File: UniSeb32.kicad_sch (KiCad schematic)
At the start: 55 parts, among them J1 IO, J101 Micro_SD_Card_Det, J2 ARJM11C7-114-BA-EW2, J3 Conn_02x05_Odd_Even, J6 SDS011, J7 Conn_01x02_Female, J8 Conn_01x02_Female, U1 mini_esp32, U101 RTL8201F-VB-CG, U3 AMS1117-3.3, U4 AMS5915, U5 module_bme280, U6 RT9400, U7 MCP23008-xSS, U8 HLK-PM01, X1 233-508, X2 233-503, X3 233-504

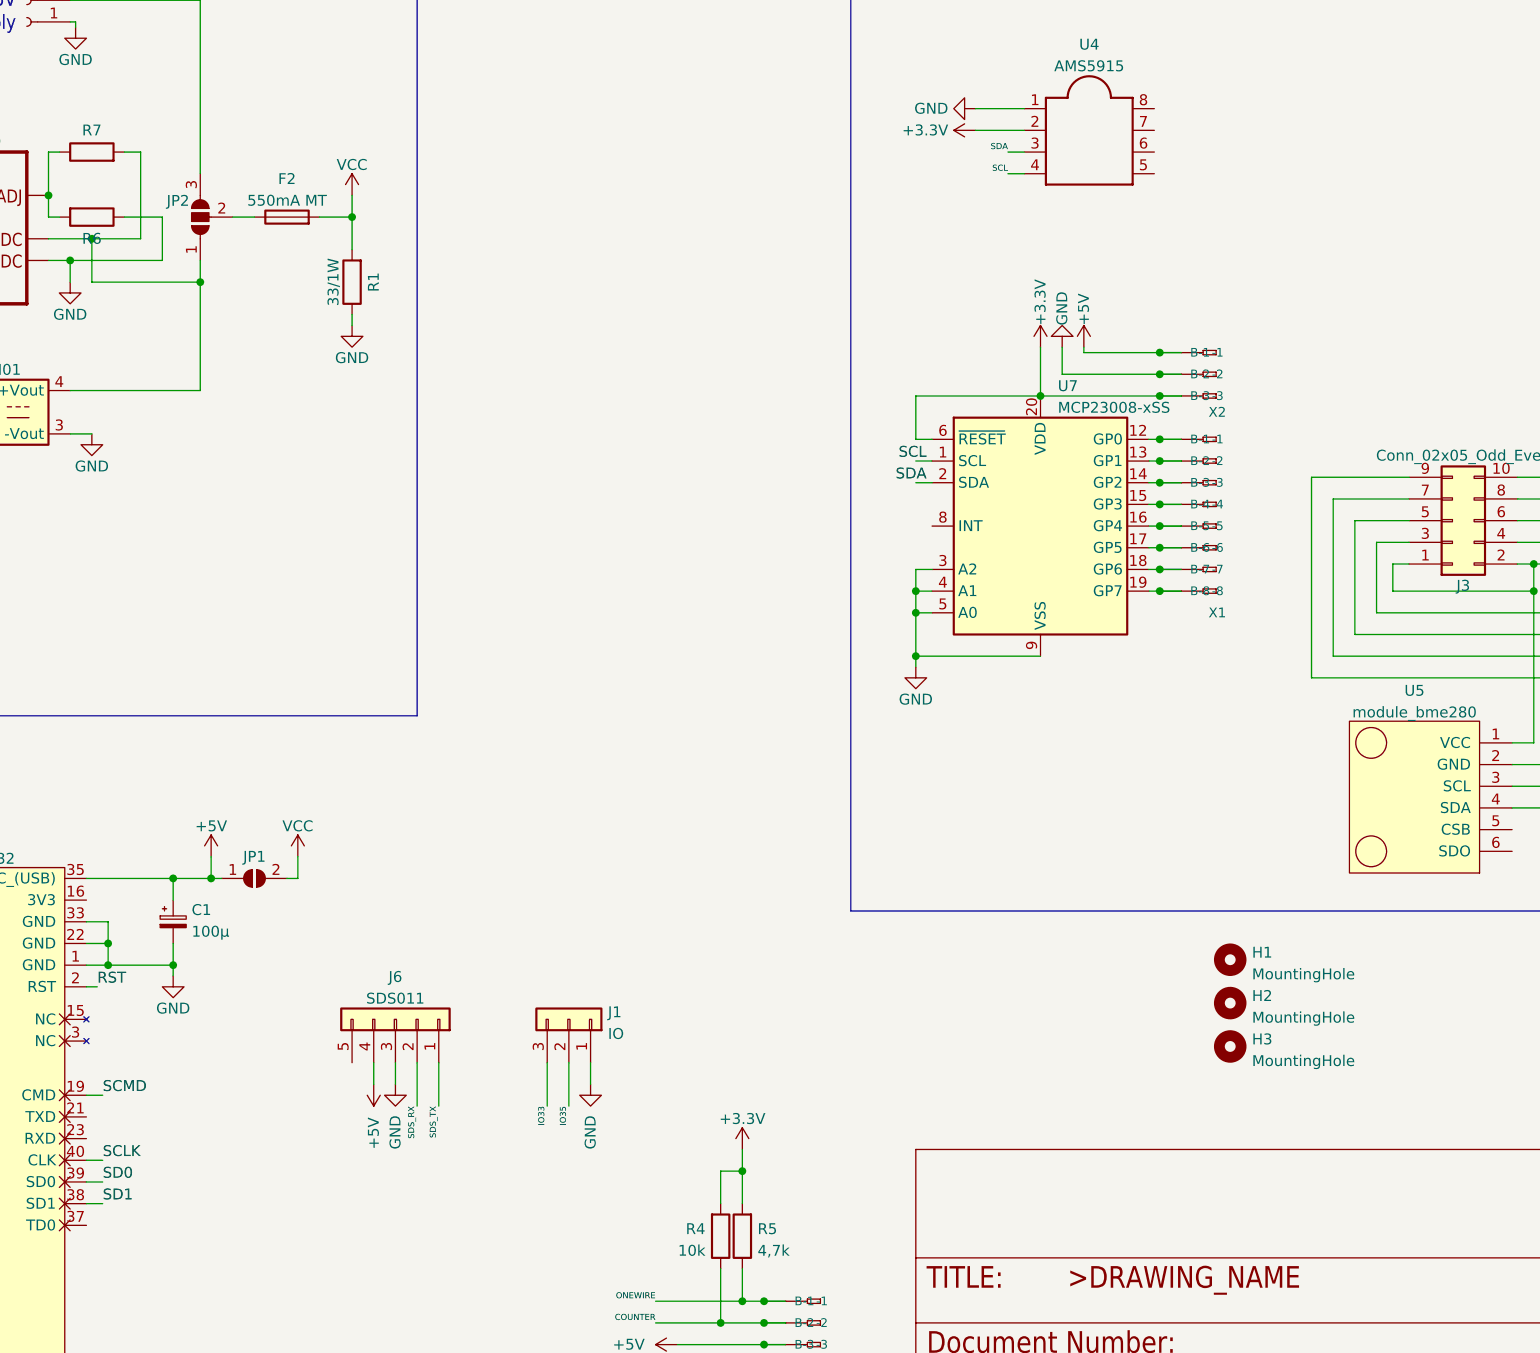
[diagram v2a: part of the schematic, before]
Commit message: removed SJ1, rename SJ2 -> SJ1, added SJ2 to change pin2 usage of J1
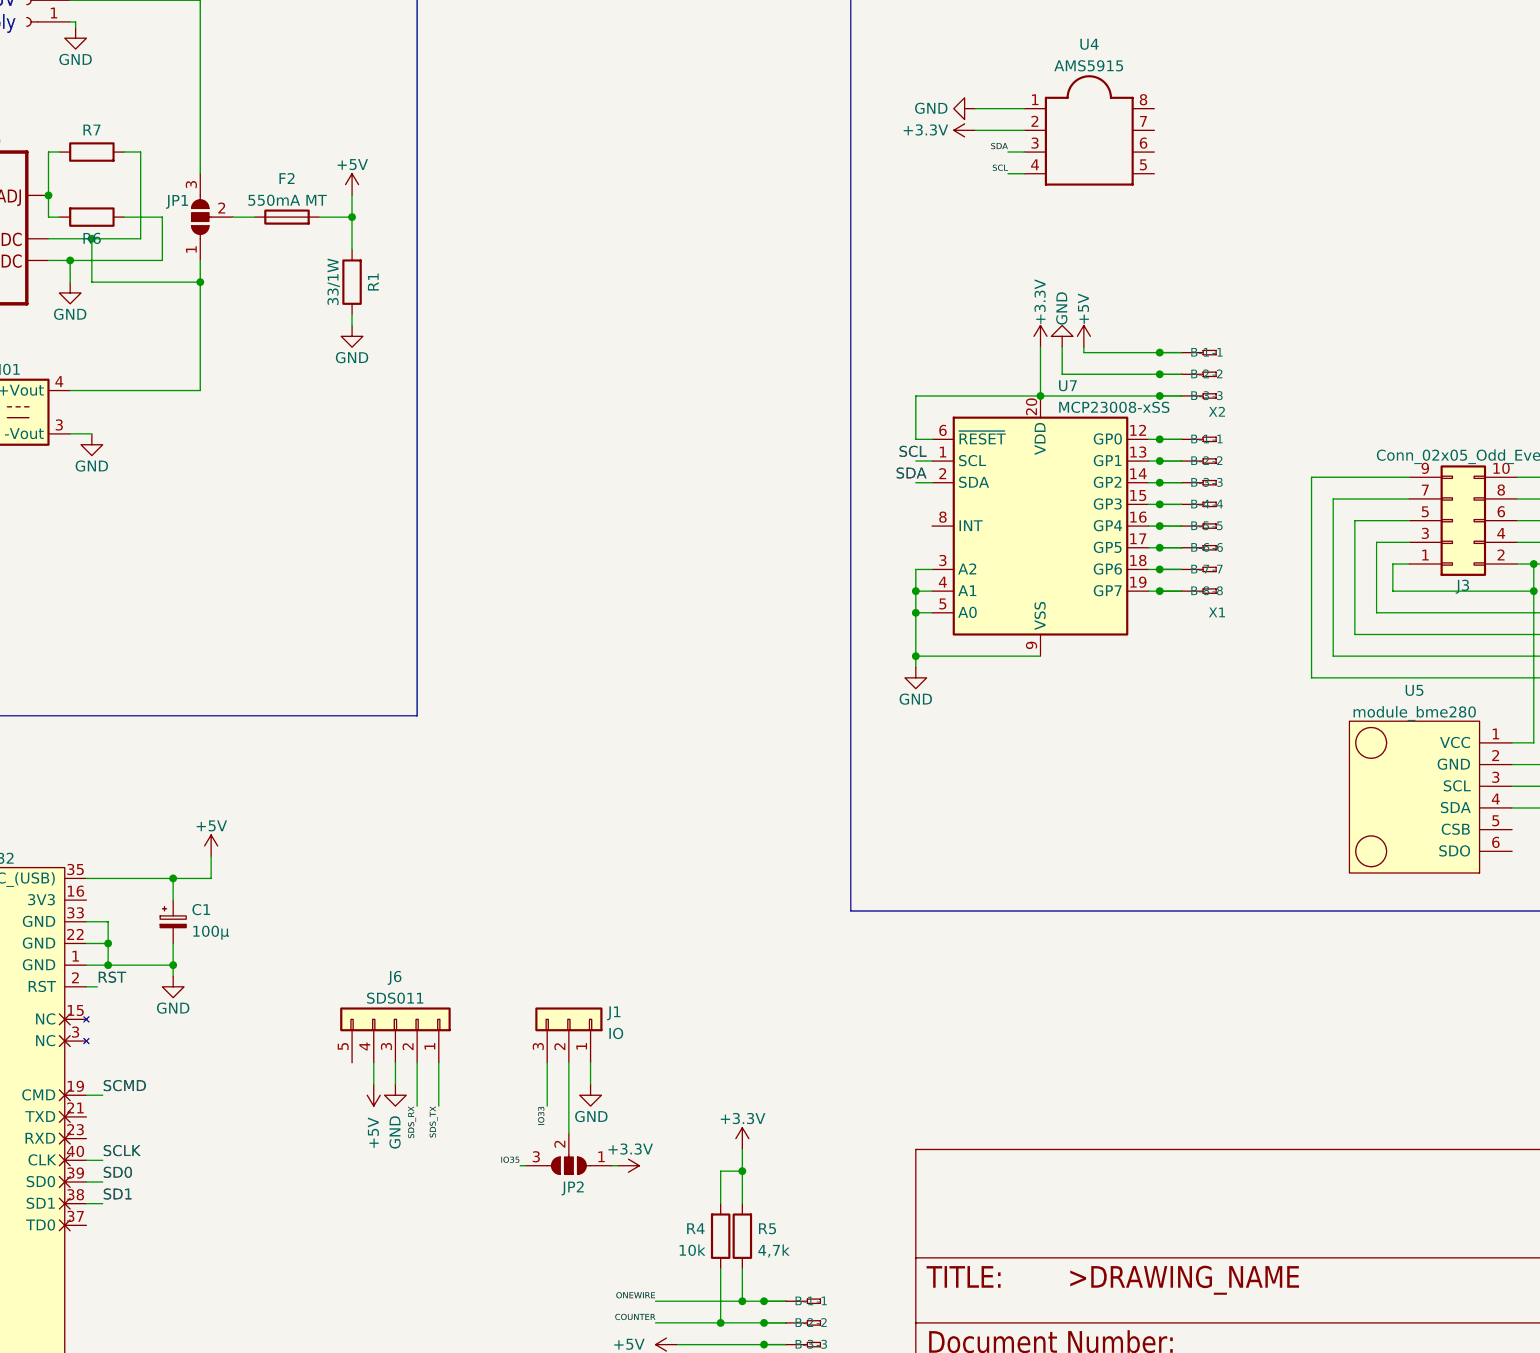
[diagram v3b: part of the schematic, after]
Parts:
- removed H1, H2, H3: MountingHole, MountingHole:MountingHole_3.2mm_M3, symbol Mechanical:MountingHole
- removed JP1: SolderJumper_2_Open, Jumper:SolderJumper-2_P1.3mm_Open_Pad1.0x1.5mm, symbol Jumper:SolderJumper_2_Open
- added JP2: SolderJumper_3_Open, Jumper:SolderJumper-3_P1.3mm_Open_Pad1.0x1.5mm_NumberLabels, symbol Jumper:SolderJumper_3_Open
- renumbered JP2 to JP1
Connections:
- net VCC is gone; now on net +5V: F2.2, R1.2
- net +3.3V: now also JP2.1 (A)
- net IO35: now also JP2.3 (B); no longer J1.2 (Pin_2)
- new net: J1.2 (Pin_2), JP2.2 (C)

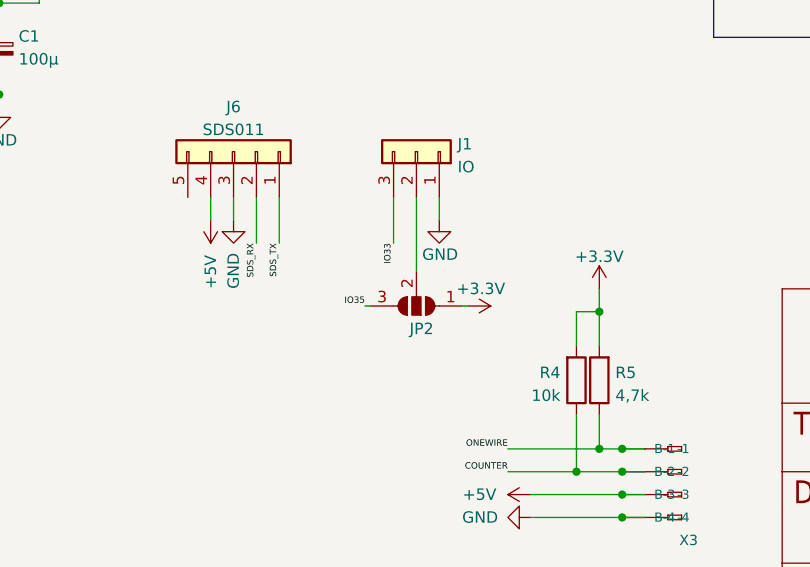
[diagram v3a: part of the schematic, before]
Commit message: added pullup for pin3 of J1
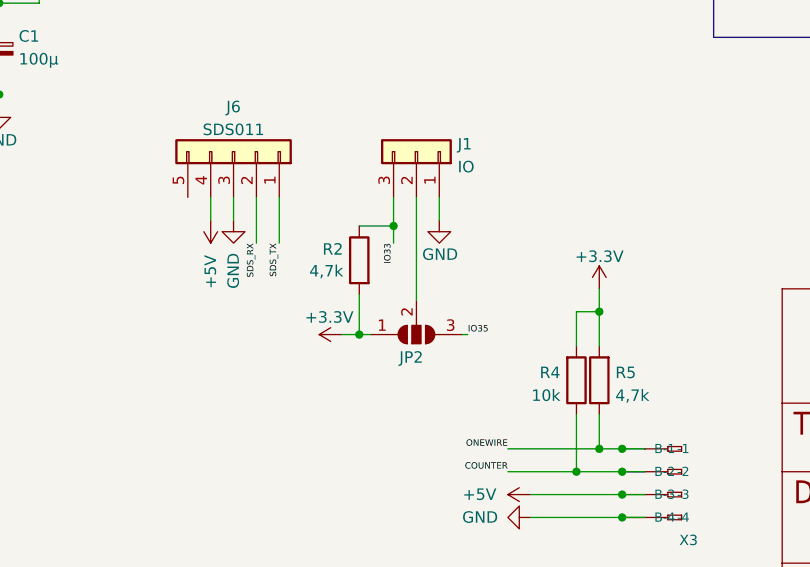
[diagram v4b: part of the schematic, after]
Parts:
- added R2: 4,7k, Resistor_SMD:R_0603_1608Metric, symbol Device:R
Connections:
- net +3.3V: now also R2.2
- net IO33: now also R2.1
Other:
- moved on the sheet: JP2
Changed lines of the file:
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@@
   (junction (at 124.46 259.08) (diameter 0) (color 0 0 0 0)
   )
+  (junction (at 133.35 167.64) (diameter 0) (color 0 0 0 0)
+  )
   (junction (at 260.35 86.36) (diameter 0) (color 0 0 0 0)
   )
@@
   (junction (at 78.74 50.8) (diameter 0) (color 0 0 0 0)
   )
+  (junction (at 137.16 155.575) (diameter 0) (color 0 0 0 0)
+  )
   (junction (at 208.915 97.155) (diameter 0) (color 0 0 0 0)
   )
@@
     (stroke (width 0) (type default))
   )
-  (wire (pts (xy 145.415 164.465) (xy 144.78 164.465))
+  (wire (pts (xy 131.445 167.64) (xy 133.35 167.64))
     (stroke (width 0) (type default))
   )
@@
     (stroke (width 0) (type default))
   )
+  (wire (pts (xy 133.35 155.575) (xy 137.16 155.575))
+    (stroke (width 0) (type default))
+  )
   (wire (pts (xy 173.355 269.24) (xy 173.355 273.685))
     (stroke (width 0) (type default))
   )
+  (wire (pts (xy 133.35 167.64) (xy 134.62 167.64))
+    (stroke (width 0) (type default))
+  )
   (wire (pts (xy 145.415 280.67) (xy 152.4 280.67))
     (stroke (width 0) (type default))
@@
     (stroke (width 0) (type default))
   )
-  (wire (pts (xy 139.7 152.4) (xy 139.7 160.655))
+  (wire (pts (xy 139.7 152.4) (xy 139.7 163.83))
     (stroke (width 0) (type default))
   )
@@
     (stroke (width 0) (type default))
   )
-  (wire (pts (xy 133.985 164.465) (xy 134.62 164.465))
+  (wire (pts (xy 145.415 167.64) (xy 144.78 167.64))
     (stroke (width 0) (type default))
   )
@@
     (stroke (width 0) (type default))
   )
-  (wire (pts (xy 137.16 152.4) (xy 137.16 157.48))
+  (wire (pts (xy 137.16 152.4) (xy 137.16 155.575))
     (stroke (width 0) (type default))
   )
@@
     (stroke (width 0) (type default))
   )
+  (wire (pts (xy 133.35 163.195) (xy 133.35 167.64))
+    (stroke (width 0) (type default))
+  )
   (wire (pts (xy 53.975 179.07) (xy 56.515 179.07))
     (stroke (width 0) (type default))
@@
     (stroke (width 0) (type default))
   )
+  (wire (pts (xy 137.16 155.575) (xy 137.16 157.48))
+    (stroke (width 0) (type default))
+  )
   (wire (pts (xy 137.16 335.915) (xy 137.16 337.185))
     (stroke (width 0) (type default))
@@
     (effects (font (size 1.27 1.27)) (justify left bottom))
   )
-  (label "IO35" (at 133.985 164.465 180) (fields_autoplaced)
-    (effects (font (size 0.7112 0.7112)) (justify right bottom))
+  (label "IO35" (at 145.415 167.64 0) (fields_autoplaced)
+    (effects (font (size 0.7112 0.7112)) (justify left bottom))
   )
   (label "IO0" (at 55.245 130.81 180) (fields_autoplaced)
@@
     )
   )
-  (symbol (lib_id "Jumper:SolderJumper_3_Open") (at 139.7 164.465 180) (unit 1)
+  (symbol (lib_id "Jumper:SolderJumper_3_Open") (at 139.7 167.64 0) (mirror x) (unit 1)
     (in_bom yes) (on_board yes) (dnp no)
-    (property "Reference" "JP2" (at 141.605 167.005 0)
+    (property "Reference" "JP2" (at 137.795 170.18 0)
       (effects (font (size 1.27 1.27)) (justify left))
     )
-    (property "Value" "SolderJumper_3_Open" (at 141.4022 166.1159 90)
+    (property "Value" "SolderJumper_3_Open" (at 137.9978 169.2909 90)
       (effects (font (size 1.27 1.27)) (justify left) hide)
     )
-    (property "Footprint" "Jumper:SolderJumper-3_P1.3mm_Open_Pad1.0x1.5mm_NumberLabels" (at 139.7 164.465 0)
+    (property "Footprint" "Jumper:SolderJumper-3_P1.3mm_Open_Pad1.0x1.5mm_NumberLabels" (at 139.7 167.64 0)
       (effects (font (size 1.27 1.27)) hide)
     )
-    (property "Datasheet" "~" (at 139.7 164.465 0)
+    (property "Datasheet" "~" (at 139.7 167.64 0)
       (effects (font (size 1.27 1.27)) hide)
     )
@@
     )
   )
-  (symbol (lib_id "power:+3.3V") (at 145.415 164.465 270) (unit 1)
+  (symbol (lib_id "power:+3.3V") (at 131.445 167.64 90) (mirror x) (unit 1)
     (in_bom yes) (on_board yes) (dnp no)
-    (property "Reference" "#PWR03" (at 141.605 164.465 0)
+    (property "Reference" "#PWR03" (at 135.255 167.64 0)
       (effects (font (size 1.27 1.27)) hide)
     )
-    (property "Value" "+3.3V" (at 144.145 162.56 90)
+    (property "Value" "+3.3V" (at 132.715 165.735 90)
       (effects (font (size 1.27 1.27)) (justify left))
     )
-    (property "Footprint" "" (at 145.415 164.465 0)
+    (property "Footprint" "" (at 131.445 167.64 0)
       (effects (font (size 1.27 1.27)) hide)
     )
-    (property "Datasheet" "" (at 145.415 164.465 0)
+    (property "Datasheet" "" (at 131.445 167.64 0)
       (effects (font (size 1.27 1.27)) hide)
     )
@@
         )
       )
+    )
+  )
+  (symbol (lib_id "Device:R") (at 133.35 159.385 0) (mirror y) (unit 1)
+    (in_bom yes) (on_board yes) (dnp no)
+    (property "Reference" "R2" (at 131.572 158.1729 0)
+      (effects (font (size 1.27 1.27)) (justify left))
+    )
+    (property "Value" "4,7k" (at 131.572 160.5971 0)
+      (effects (font (size 1.27 1.27)) (justify left))
+    )
+    (property "Footprint" "Resistor_SMD:R_0603_1608Metric" (at 135.128 159.385 90)
+      (effects (font (size 1.27 1.27)) hide)
+    )
+    (property "Datasheet" "~" (at 133.35 159.385 0)
+      (effects (font (size 1.27 1.27)) hide)
+    )
+    (property "LCSC" "C23162" (at 133.35 159.385 90)
+      (effects (font (size 1.27 1.27)) hide)
+    )
+    (property "JLC" "0603" (at 133.35 159.385 0)
+      (effects (font (size 1.27 1.27)) hide)
+    )
+    (pin "1")
+    (pin "2")
+    (instances
+      (project "UniSeb32"
+        (path "/94c30dae-83f2-410e-815e-9e5d06243376"
+          (reference "R2") (unit 1)
+        )
+      )

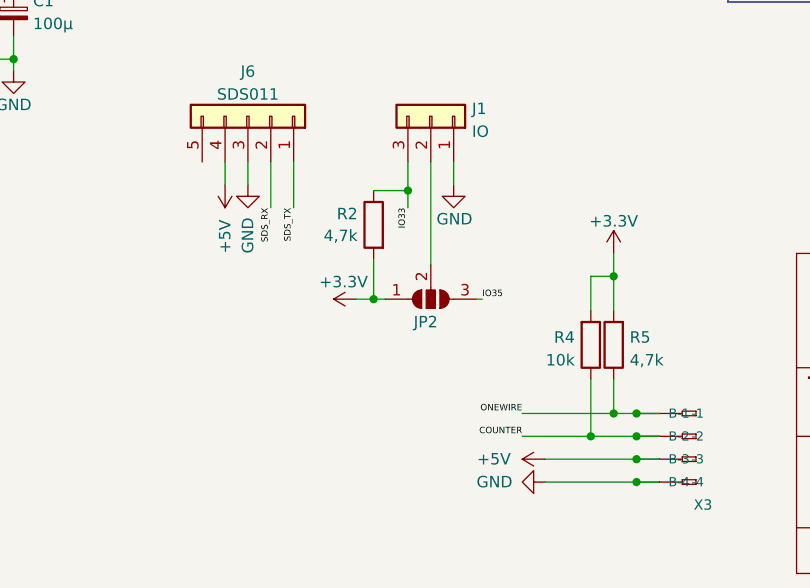
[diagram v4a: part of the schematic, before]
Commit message: Changed JP2-fixed voltage option (3.3V) to flexible voltage (3.3V/5V) with JP3
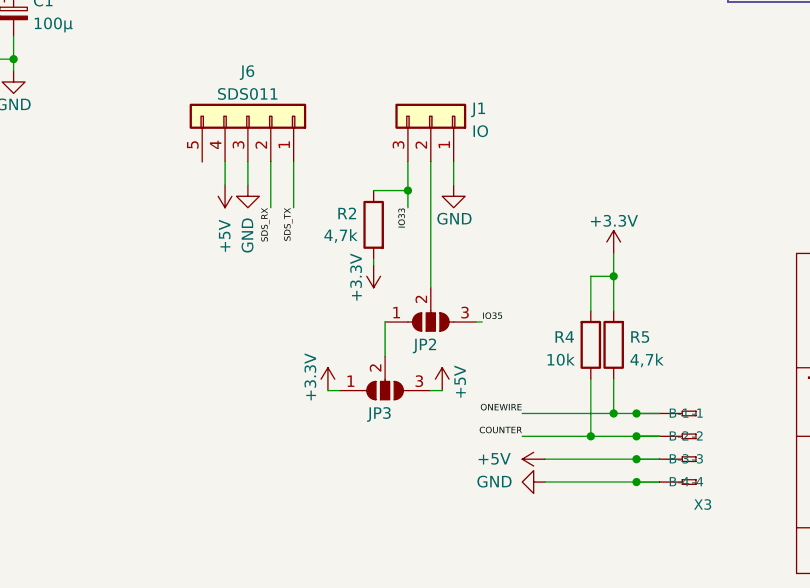
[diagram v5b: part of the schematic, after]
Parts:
- added JP3: SolderJumper_3_Open, Jumper:SolderJumper-3_P1.3mm_Open_Pad1.0x1.5mm_NumberLabels, symbol Jumper:SolderJumper_3_Open
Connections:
- net +3.3V: now also JP3.1 (A); no longer JP2.1 (A)
- net +5V: now also JP3.3 (B)
- new net: JP2.1 (A), JP3.2 (C)
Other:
- moved on the sheet: JP2
